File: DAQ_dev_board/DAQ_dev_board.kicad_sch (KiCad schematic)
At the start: 6 parts, among them U1 ADS1158IRTCR, Y1 32.768kHz

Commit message: updated schematic
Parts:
- added D2: LED, symbol Device:LED
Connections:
- net GND: now also D1.1 (K), D2.1 (K)
- net +5V: now reaches U1.28 (DVDD)
- net +5V: now also U1.6 (AVDD), D2.2 (A)
- no-connect marks 0 -> 2

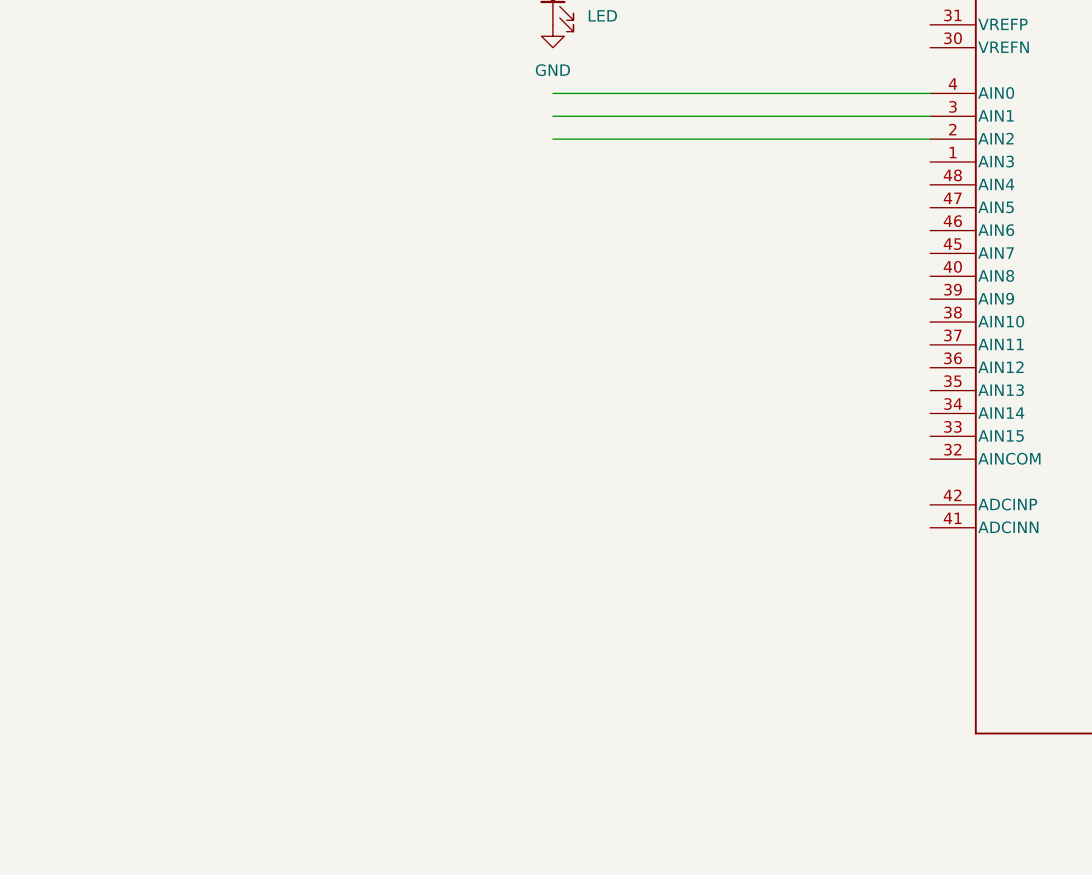
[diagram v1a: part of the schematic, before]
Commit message: Added TC Chip
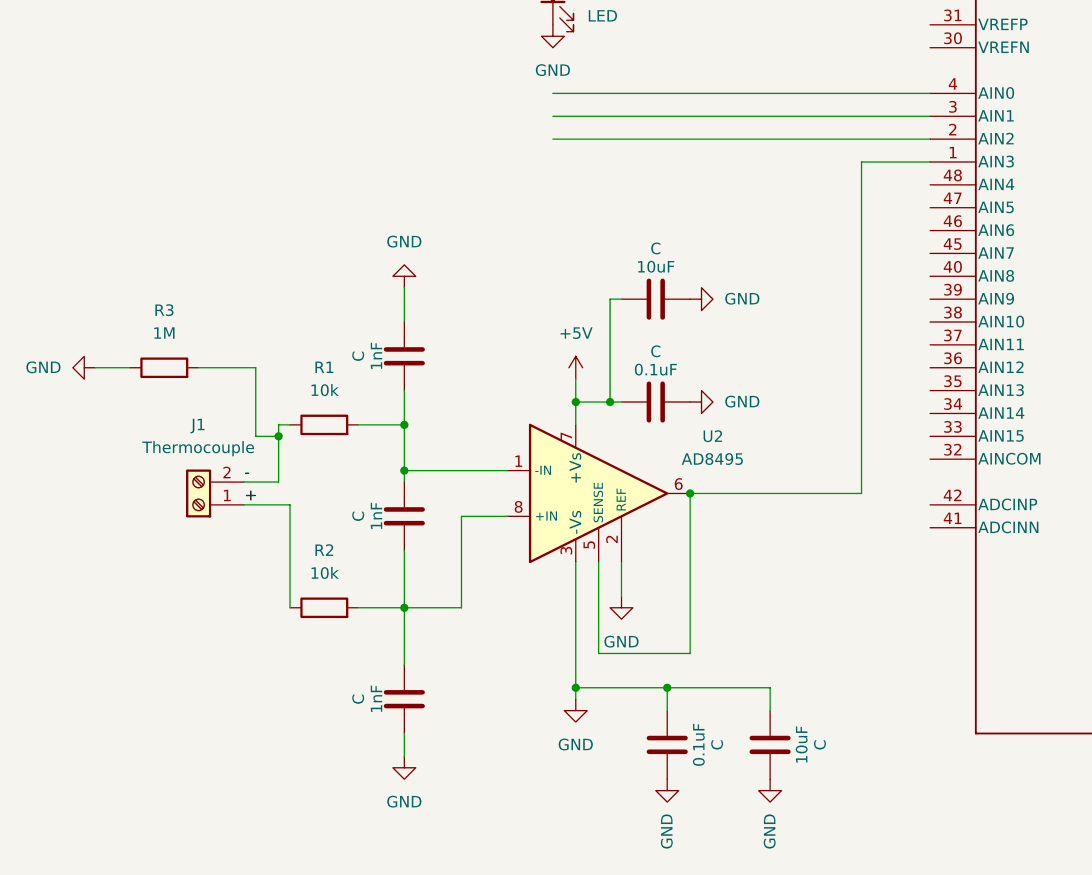
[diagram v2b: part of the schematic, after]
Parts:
- added 0.1uF (x2), 10uF (x2), 1nF (x3): C, symbol Device:C
- added J1: Thermocouple, symbol Connector:Screw_Terminal_01x02
- added R1, R2: 10k, symbol Device:R
- added R3: 1M, symbol Device:R
- added U2: AD8495, Package_SO:MSOP-8_3x3mm_P0.65mm, symbol Sensor_Temperature:AD8495
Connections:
- net +5V: now also 0.1uF.2, 10uF.2, U2.7 (+Vs)
- net GND: now also 0.1uF.1, 0.1uF.1, 0.1uF.2, 10uF.1, 10uF.1, 10uF.2, 1nF.1, 1nF.2, R3.1, U2.2 (REF), U2.3 (-Vs)
- net at U1.1 (AIN3): now also U2.5 (SENSE), U2.6
- new net: 1nF.1, 1nF.2, R1.2, U2.1 (-IN)
- new net: 1nF.1, 1nF.2, R2.2, U2.8 (+IN)
- new net +: J1.1 (Pin_1), R2.1
- new net -: J1.2 (Pin_2), R1.1, R3.2

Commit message: updated ADC board
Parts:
- added J2: A0, A1, symbol Connector:Screw_Terminal_01x02
- added J3: GPIO1, GPIO2, symbol Connector:Screw_Terminal_01x02
- added J4: CS, DRDY, symbol Connector:Screw_Terminal_01x02
- added J5: SCLK, DIN, symbol Connector:Screw_Terminal_01x02
- added J6: DOUT, START, symbol Connector:Screw_Terminal_01x02
- added J7: RESET, PDWN, symbol Connector:Screw_Terminal_01x02
- added R4, R5: 1k, symbol Device:R_US
- added U3: OP777ARZ (OP AMP), R_8_ADI, symbol OP777:OP777ARZ
- R1, R2, R3: symbol Device:R -> Device:R_US
- U1: value ADS1158IRTCR -> ADS1158IRTCR (ADC)
- U2: value AD8495 -> AD8495 (TC AMP)
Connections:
- net +5V: now also R5.1, U3.7 (V+)
- net GND: now also R4.2, U3.4 (V-); no longer U2.2 (REF)
- net at U2.5 (SENSE), U2.6: now also U1.2 (AIN2); no longer U1.1 (AIN3)
- net at U1.10 (PWDN_N): now also J7.2 (Pin_2)
- net at U1.11 (RESET_N): now also J7.1 (Pin_1)
- net at U1.15 (GPIO1): now also J3.1 (Pin_1)
- net at U1.16 (GPIO2): now also J3.2 (Pin_2)
- net at U1.22 (SCLK): now also J5.1 (Pin_1)
- net at U1.23 (DIN): now also J5.2 (Pin_2)
- net at U1.24 (DOUT): now also J6.1 (Pin_1)
- net at U1.25 (DRDY_N): now also J4.2 (Pin_2)
- net at U1.26 (START): now also J6.2 (Pin_2)
- net at U1.27 (CS_N): now also J4.1 (Pin_1)
- net at U1.3 (AIN1): now also J2.1 (Pin_1)
- net at U1.4 (AIN0): now also J2.2 (Pin_2)
- new net: R4.1, R5.2, U3.3 (IN+)
- new net: U2.2 (REF), U3.6 (OUT)
- no-connect marks 2 -> 20
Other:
- moved on the sheet: 0.1uF, 10uF, 1nF, C1, C2, C3, D1, D2, J1, U1, U2, Y1

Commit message: taylor D comments plz contact me if Qs
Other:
- note added: "TaylorD : dont have wires overlap like this"
- note added: "bad practice"
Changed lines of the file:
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@@
+		)
+	)
+	(rectangle
+		(start 172.72 102.87)
+		(end 203.2 118.11)
+		(stroke
+			(width 0)
+			(type default)
+		)
+		(fill
+			(type none)
+		)
+	)
+	(rectangle
+		(start 60.96 110.49)
+		(end 67.31 116.84)
+		(stroke
+			(width 0)
+			(type default)
+		)
+		(fill
+			(type none)
+		)
+	)
+	(rectangle
+		(start 27.94 163.83)
+		(end 58.42 168.91)
+		(stroke
+			(width 0)
+			(type default)
+		)
+		(fill
+			(type none)
+		)
+	)
+	(rectangle
+		(start 43.18 44.45)
+		(end 85.09 52.07)
+		(stroke
+			(width 0)
+			(type default)
+		)
+		(fill
+			(type none)
+		)
+	)
+	(rectangle
+		(start 168.91 30.48)
+		(end 175.26 36.83)
+		(stroke
+			(width 0)
+			(type default)
+		)
+		(fill
+			(type none)
+		)
+	)
+	(rectangle
+		(start 163.83 99.06)
+		(end 170.18 106.68)
+		(stroke
+			(width 0)
+			(type default)
+		)
+		(fill
+			(type none)
+		)
+	)
+	(text "bad practice "
+		(exclude_from_sim no)
+		(at 43.18 166.37 0)
+		(effects
+			(font
+				(size 1.27 1.27)
+			)
+		)
+	)
+	(text "TaylorD : dont have wires overlap like this "
+		(exclude_from_sim no)
+		(at 190.5 114.808 0)
+		(effects
+			(font
+				(size 1.016 1.016)
+			)
+		)
+	)
+	(text "bad practice "
+		(exclude_from_sim no)
+		(at 62.23 49.022 0)
+		(effects
+			(font
+				(size 1.27 1.27)
+			)
+		)
+	)
+	(text "bad practice "
+		(exclude_from_sim no)
+		(at 167.894 99.822 0)
+		(effects
+			(font
+				(size 1.27 1.27)
+			)
+		)
+	)
+	(text "bad practice "
+		(exclude_from_sim no)
+		(at 65.024 115.316 0)
+		(effects
+			(font
+				(size 1.27 1.27)
+			)
 		)
 	)

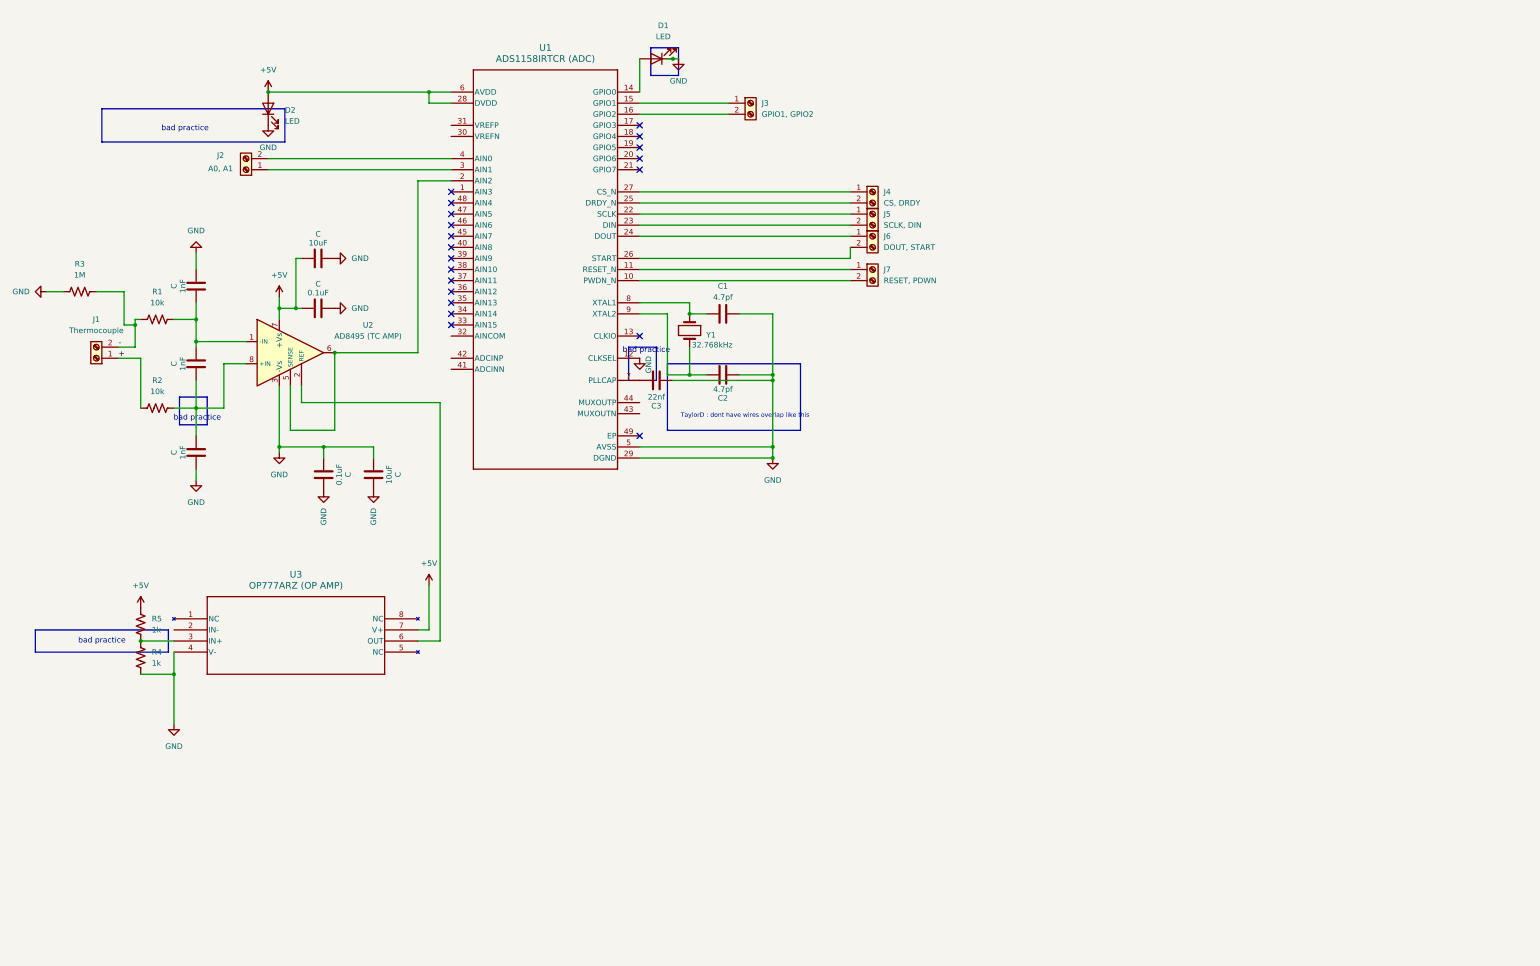
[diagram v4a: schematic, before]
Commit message: schematic updates + formatting fixes
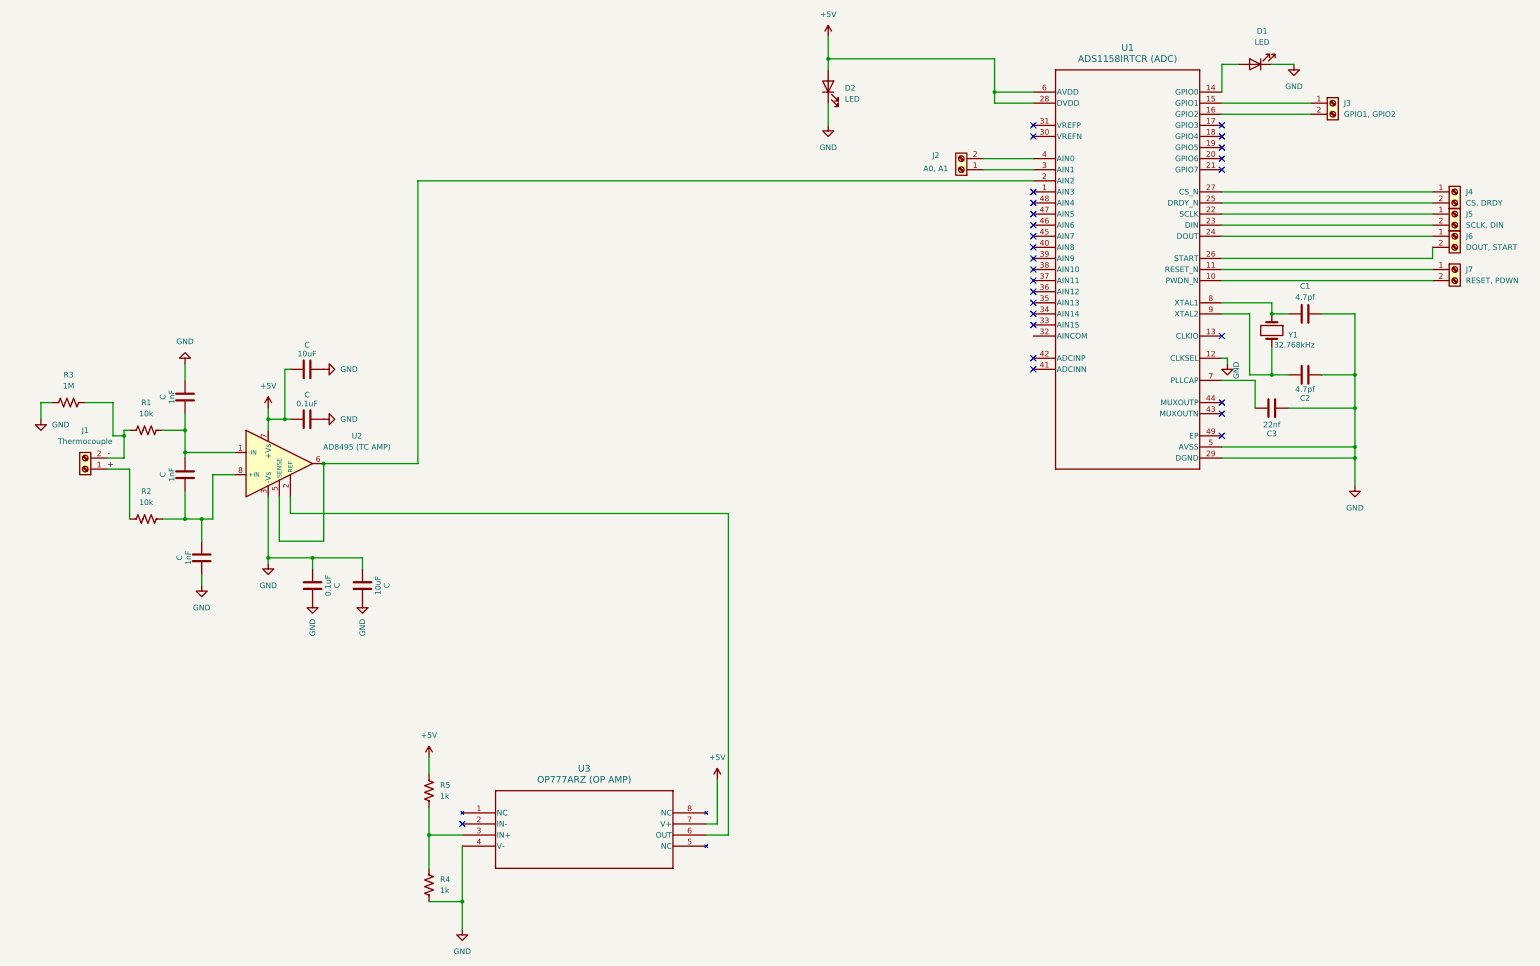
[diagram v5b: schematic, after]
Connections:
- no-connect marks 20 -> 27
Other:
- note removed: "TaylorD : dont have wires overlap like this"
- note removed: "bad practice"
- moved on the sheet: 0.1uF, 10uF, 1nF, C1, C2, C3, D2, J1, J2, J3, J4, J5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

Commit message: updated op amp to be a buffer and added flags
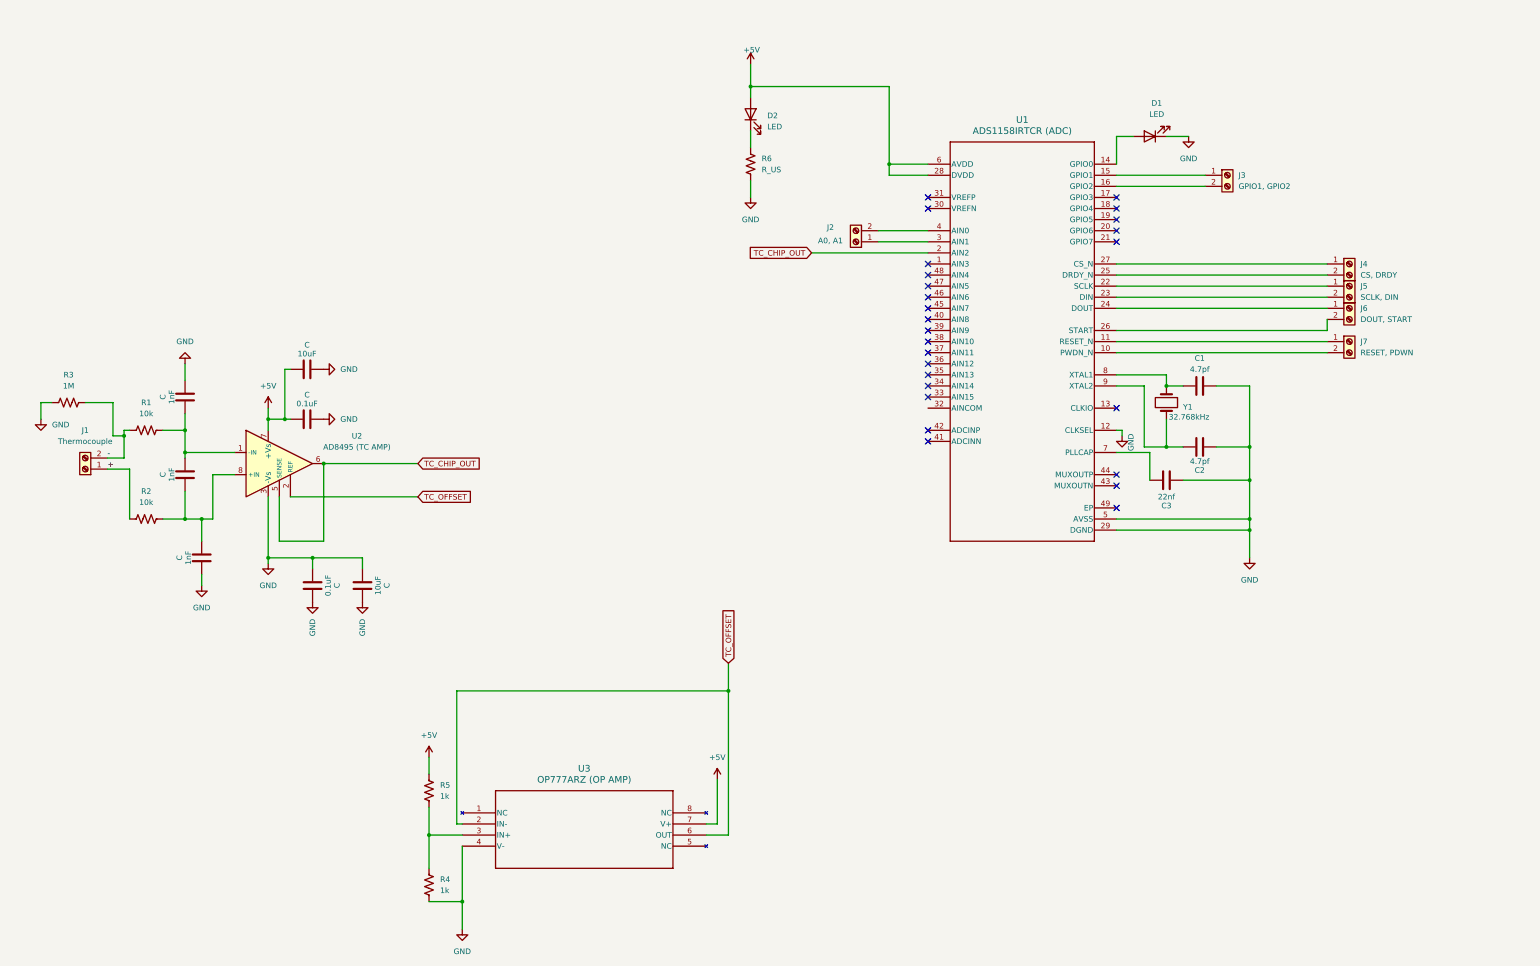
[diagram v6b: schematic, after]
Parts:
- added R6: R_US, symbol Device:R_US
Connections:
- net GND: now also R6.2; no longer D2.1 (K)
- net TC_OFFSET: now reaches U3.2 (IN-)
- net TC_OFFSET: now also U2.2 (REF), U3.6 (OUT)
- net TC_CHIP_OUT: now reaches U1.2 (AIN2), U2.5 (SENSE), U2.6
- new net: D2.1 (K), R6.1
- no-connect marks 27 -> 26
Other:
- moved on the sheet: C1, C2, C3, D1, D2, J2, J3, J4, J5, J6, J7, U1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

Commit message: updated resistors and adding footprints
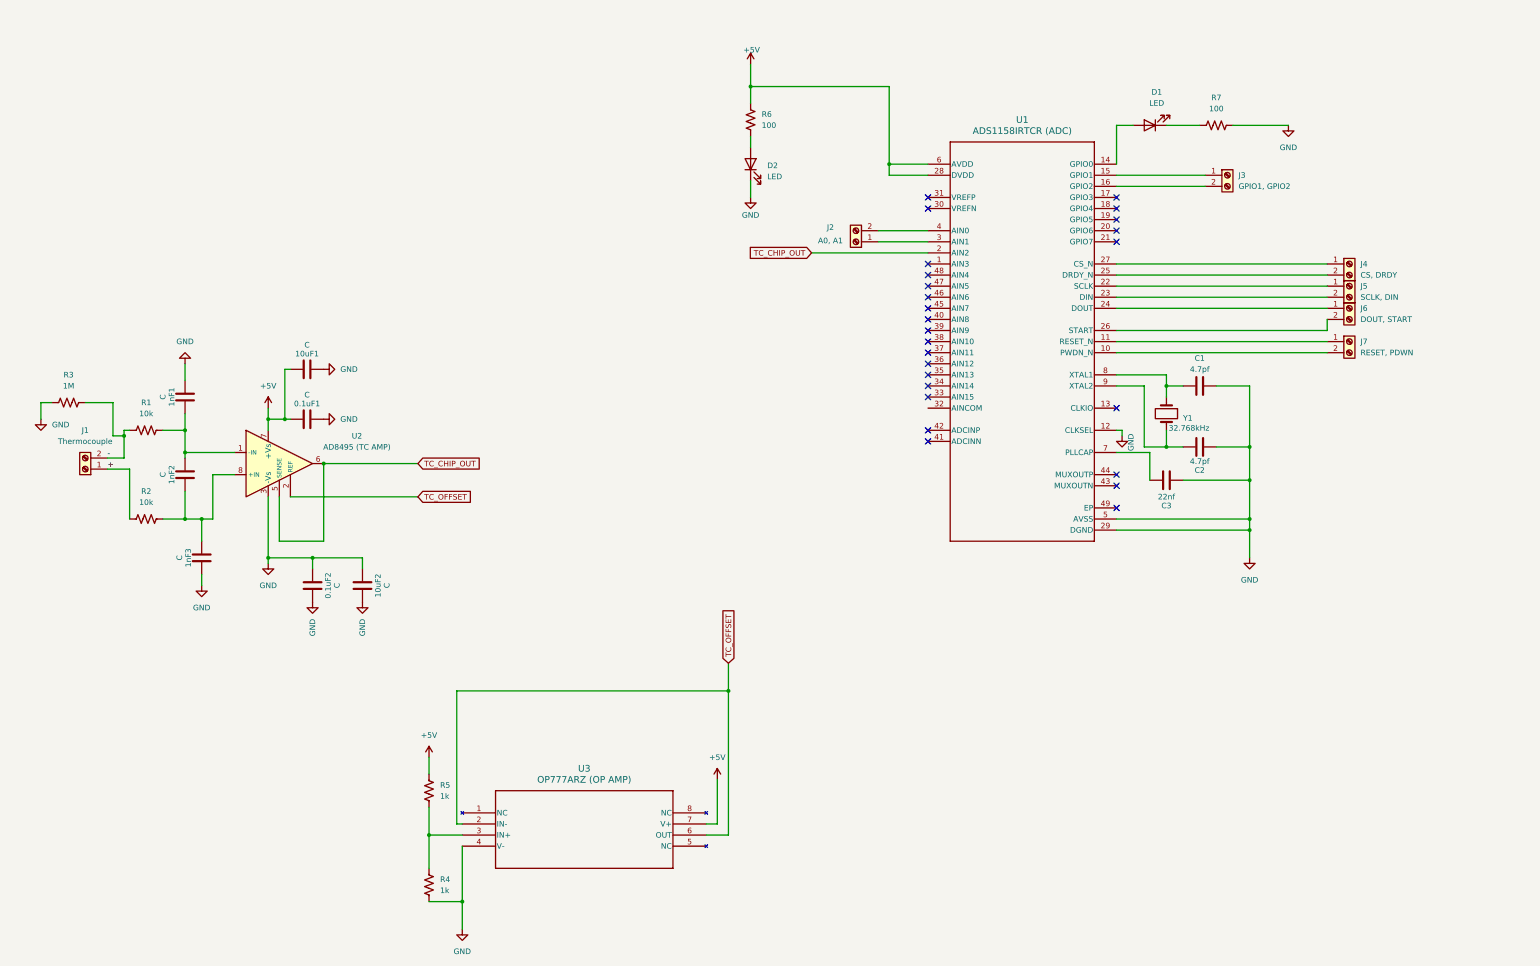
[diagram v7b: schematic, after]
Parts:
- added R7: 100, Capacitor_SMD:C_0603_1608Metric, symbol Device:R_US
- 0.1uF1, 0.1uF2: renamed from 0.1uF; footprint (none) -> Capacitor_SMD:C_0603_1608Metric
- 10uF1, 10uF2: renamed from 10uF; footprint (none) -> Capacitor_SMD:C_0603_1608Metric
- 1nF1, 1nF2, 1nF3: renamed from 1nF; footprint (none) -> Capacitor_SMD:C_0603_1608Metric
- C1, C2, C3, D1, D2, R1, R2, R3, R4, R5: footprint (none) -> Capacitor_SMD:C_0603_1608Metric
- J2, J3, J4, J5, J6, J7: footprint (none) -> Connector_PinHeader_2.54mm:PinHeader_1x01_P2.54mm_Vertical
- R6: value R_US -> 100; footprint (none) -> Capacitor_SMD:C_0603_1608Metric
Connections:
- net +5V: now also R6.1; no longer D2.2 (A)
- net GND: now also D2.1 (K), R7.2; no longer D1.1 (K), R6.2
- new net: D2.2 (A), R6.2
- new net: D1.1 (K), R7.1
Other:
- moved on the sheet: D1, Y1
